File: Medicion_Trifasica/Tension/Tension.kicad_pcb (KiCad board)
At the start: 4 copper layers, 60.5 x 22.5 mm, 14 parts, among them IC1 ADR130BUJZ-REEL7, J1 Screw_Terminal_01x02, J2 Conn_01x02_Pin, J3 Conn_01x02_Pin, T1 Transformer_220/9, U1 LM358

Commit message: Mejoras PCB medicion tension
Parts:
- moved C1 92.1 mm to (168.5, 100.3)
- moved C2 92.1 mm to (156.2, 99.2)
- moved C3 92.1 mm to (162.2, 99.2)
- moved IC1 92.1 mm to (159.2, 98.7)
- moved J1 92.1 mm to (126.3, 107.8)
- moved J3 92.1 mm to (169.3, 113.6)
- moved R1 92.1 mm to (155.0, 103.6)
- moved R2 92.1 mm to (155.0, 108.1)
- moved R3 92.1 mm to (159.0, 104.6)
- moved R4 92.1 mm to (163.0, 103.6)
- moved R5 92.1 mm to (168.5, 98.1)
- moved T1 92.1 mm to (146.8, 101.8)
- moved U1 92.1 mm to (168.6, 105.1)
- moved J2 88.3 mm to (175.1, 104.6)
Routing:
- net Net-(J2-Pin_1): track 21.1 -> 16.4 mm
- net GND: track 50.1 -> 45.4 mm
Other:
- board size 60.5 x 22.5 mm -> 55.8 x 22.5 mm

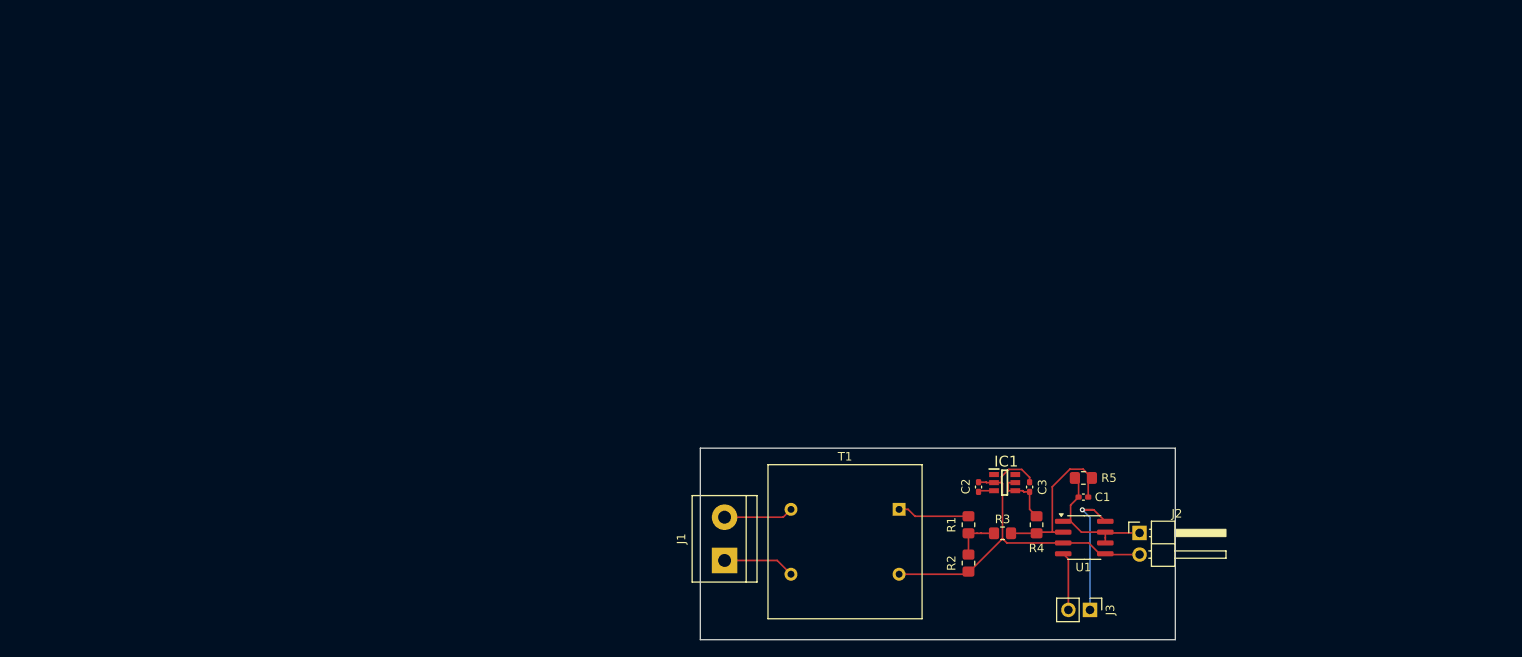
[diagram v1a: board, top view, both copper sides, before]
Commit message: Correciones PCBs
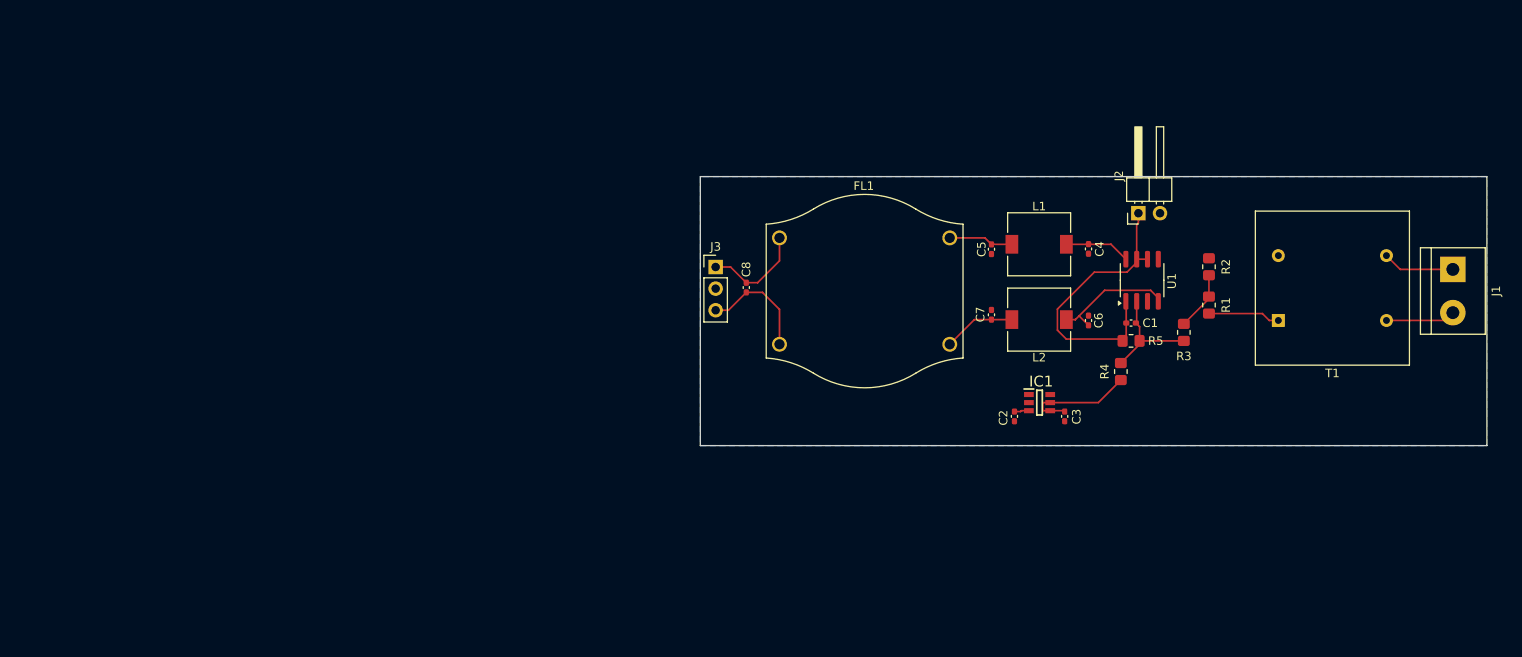
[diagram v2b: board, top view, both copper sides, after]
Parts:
- added C4: 100 nF, Capacitor_SMD:C_0402_1005Metric_Pad0.74x0.62mm_HandSolder, F.Cu at (169.1, 71.2)
- added C5: 100 nF, Capacitor_SMD:C_0402_1005Metric_Pad0.74x0.62mm_HandSolder, F.Cu at (157.7, 71.2)
- added C6: 100 nF, Capacitor_SMD:C_0402_1005Metric_Pad0.74x0.62mm_HandSolder, F.Cu at (169.1, 79.6)
- added C7: 100 nF, Capacitor_SMD:C_0402_1005Metric_Pad0.74x0.62mm_HandSolder, F.Cu at (157.7, 78.9)
- added C8: 470 uF, Capacitor_SMD:C_0402_1005Metric_Pad0.74x0.62mm_HandSolder, F.Cu at (128.9, 75.7)
- added FL1: Choke_CommonMode_FerriteCore_1234, Inductor_THT:Choke_EPCOS_B82722A, F.Cu at (132.8, 69.9)
- added L1: 30 uH, Inductor_SMD:L_7.3x7.3_H3.5, F.Cu at (163.3, 70.7)
- added L2: 30 uH, Inductor_SMD:L_7.3x7.3_H3.5, F.Cu at (163.3, 79.5)
- J3: value Conn_01x02_Pin -> Conn_01x03_Pin; footprint Connector_PinHeader_2.54mm:PinHeader_1x02_P2.54mm_Vertical -> Connector_PinHeader_2.54mm:PinHeader_1x03_P2.54mm_Vertical
- moved J1 92.1 mm to (211.9, 73.6), turned to -90 degrees
- moved J3 59.6 mm to (125.3, 73.3), turned to 0 degrees
- moved T1 49.8 mm to (191.4, 79.6), turned to 180 degrees
- moved R2 44.8 mm to (183.2, 73.3), turned to 90 degrees
- moved R1 38.3 mm to (183.2, 77.8), turned to 90 degrees
- moved J2 37.6 mm to (175.0, 67.0), turned to 90 degrees
- moved R3 31.8 mm to (180.3, 81.0), turned to -90 degrees
- moved U1 31.0 mm to (175.4, 74.9), turned to 90 degrees
- moved C1 21.2 mm to (174.1, 79.9)
- moved R4 20.5 mm to (172.9, 85.6), turned to 90 degrees
- moved R5 17.0 mm to (174.1, 82.0)
- moved IC1 10.3 mm to (163.3, 89.2)
- moved C2 9.31 mm to (160.4, 90.9), turned to -90 degrees
- moved C3 9.27 mm to (166.3, 90.9), turned to -90 degrees
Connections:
- J3 pad 2: Net-(J3-Pin_2) -> GND
- U1 pad 4: Net-(J3-Pin_2) -> Net-(U1C-V-)
- U1 pad 8: Net-(J3-Pin_1) -> +9V
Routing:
- net GND: track 45.4 -> 0.44 mm
- net Net-(J2-Pin_1): track 16.4 -> 34.1 mm
- net Net-(U1C-V-): track 0.00 -> 14.6 mm
- net Net-(J3-Pin_3): track 0.00 -> 13.3 mm
- net Net-(C7-Pad2): track 0.00 -> 8.50 mm
- net +9V: track 1.87 -> 9.67 mm
- net Net-(J3-Pin_1): track 20.5 -> 12.8 mm, vias 1 -> 0
- net Net-(C5-Pad2): track 0.00 -> 7.62 mm
- net Net-(J3-Pin_2): track 6.85 -> 0.00 mm
- net Net-(U1A--): track 19.9 -> 13.6 mm
- net VDC_0.5: track 7.65 -> 13.8 mm
- net Net-(R1-Pad2): track 5.50 -> 6.93 mm
- added copper zone on B.Cu, net GND
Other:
- board size 55.8 x 22.5 mm -> 92.4 x 31.6 mm
- copper layers 4 -> 2

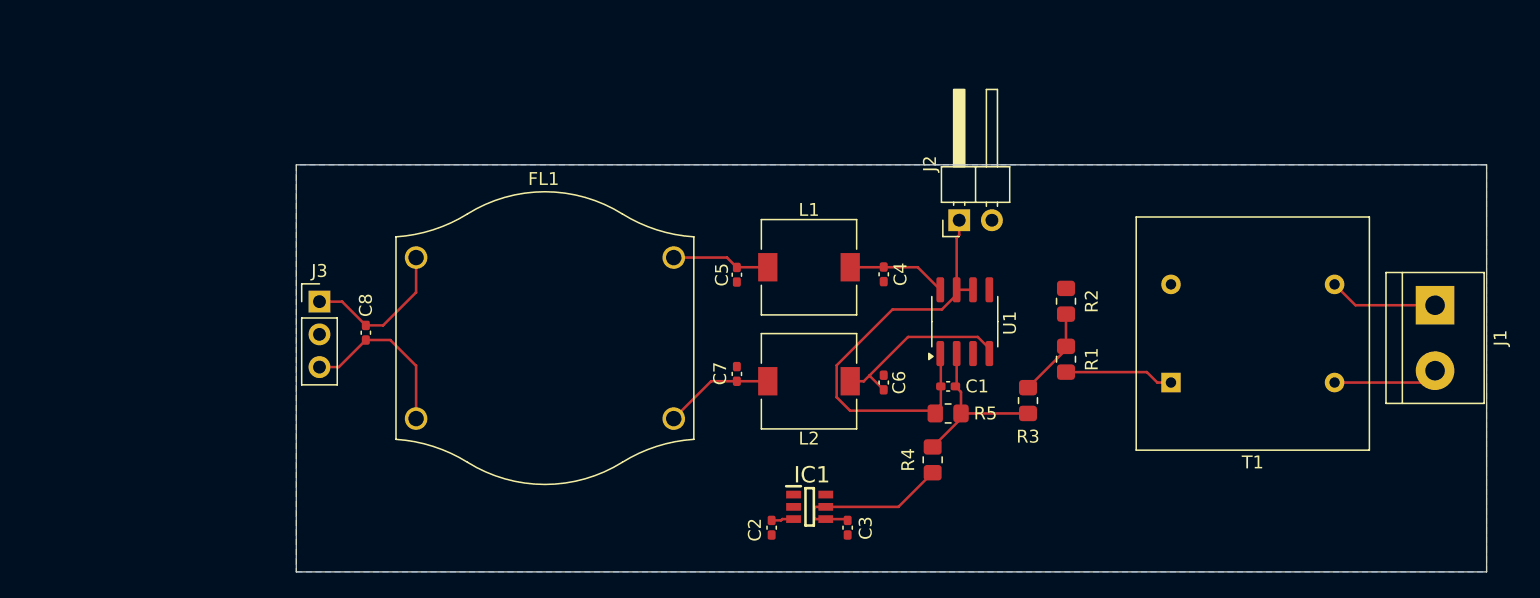
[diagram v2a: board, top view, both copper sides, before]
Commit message: Mejora en la organizacion de los circuitos con netclases y colores
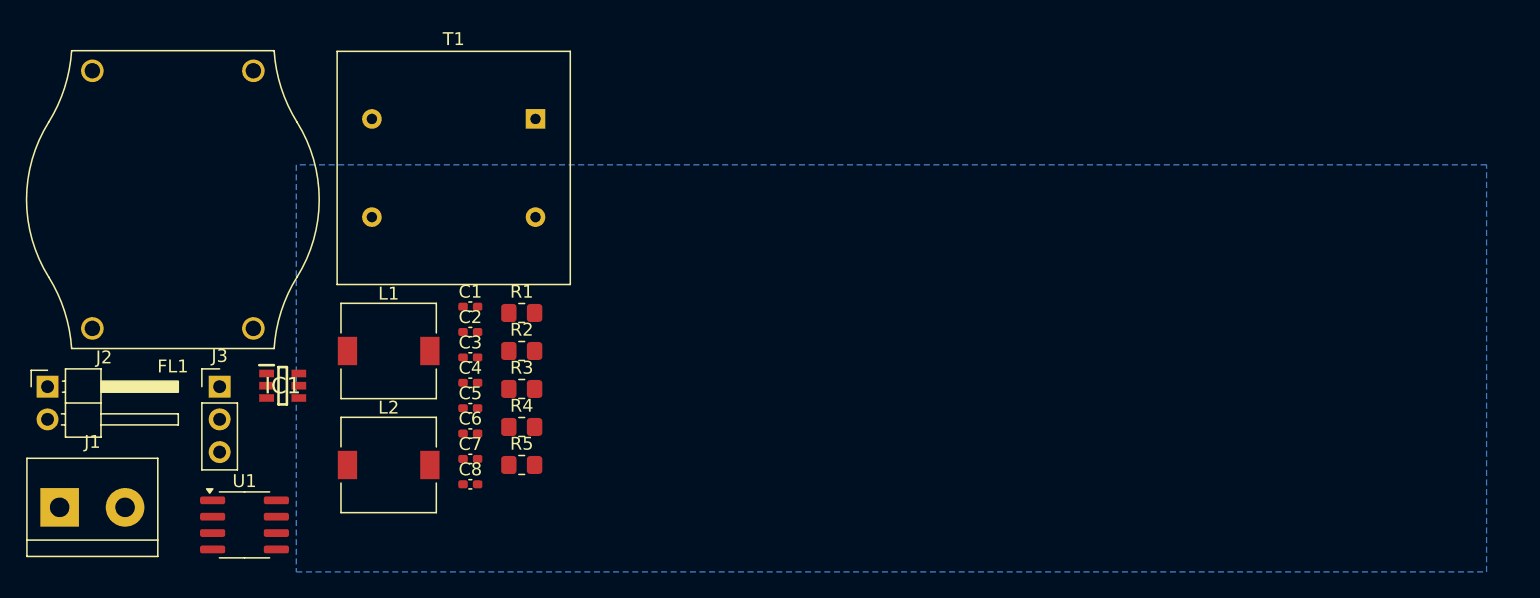
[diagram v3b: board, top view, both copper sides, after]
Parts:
- moved J1 107.9 mm to (105.1, 89.3), turned to 0 degrees
- moved J2 71.9 mm to (104.2, 79.9), turned to 0 degrees
- moved U1 58.1 mm to (119.5, 90.7), turned to 0 degrees
- moved T1 53.4 mm to (142.1, 59.1), turned to 0 degrees
- moved R2 42.4 mm to (141.0, 77.2), turned to 0 degrees
- moved R1 42.4 mm to (141.0, 74.2), turned to 0 degrees
- moved IC1 42.0 mm to (122.4, 79.8)
- moved R3 39.3 mm to (141.0, 80.1), turned to 0 degrees
- moved C1 37.6 mm to (137.0, 73.7), turned to 0 degrees
- moved R5 33.3 mm to (141.0, 86.0), turned to 0 degrees
- moved L1 33.3 mm to (130.7, 77.2)
- moved L2 33.3 mm to (130.7, 86.0), turned to 0 degrees
- moved C4 33.2 mm to (137.0, 79.6), turned to 0 degrees
- moved C6 32.3 mm to (137.0, 83.6), turned to 0 degrees
- moved C3 32.1 mm to (137.0, 77.7), turned to 0 degrees
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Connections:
- net Net-(J1-Pin_1) renamed /AC-
- net Net-(J1-Pin_2) renamed /AC+
- net Net-(J2-Pin_1) renamed /Voltage_O_Buffer
- net Net-(J3-Pin_1) renamed /Input_+9V
- net Net-(J3-Pin_3) renamed /Input_-9V
- net Net-(R1-Pad2) renamed /Voltage_Div
- net Net-(U1A--) renamed /AO_SUM_e+
- net Net-(U1C-V-) renamed /-9V
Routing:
- net /Voltage_O_Buffer: track 34.1 -> 0.00 mm
- net /-9V: track 14.6 -> 0.00 mm
- net VDC_0.5: track 13.8 -> 0.00 mm
- net /AO_SUM_e+: track 13.6 -> 0.00 mm
- net /Input_-9V: track 13.3 -> 0.00 mm
- net /Input_+9V: track 12.8 -> 0.00 mm
- net +9V: track 9.67 -> 0.00 mm
- net Net-(C7-Pad2): track 8.50 -> 0.00 mm
- net Net-(T1-SB): track 8.49 -> 0.00 mm
- net /AC-: track 8.47 -> 0.00 mm
- net /AC+: track 8.18 -> 0.00 mm
- net Net-(C5-Pad2): track 7.62 -> 0.00 mm
- net /Voltage_Div: track 6.93 -> 0.00 mm
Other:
- board outline removed

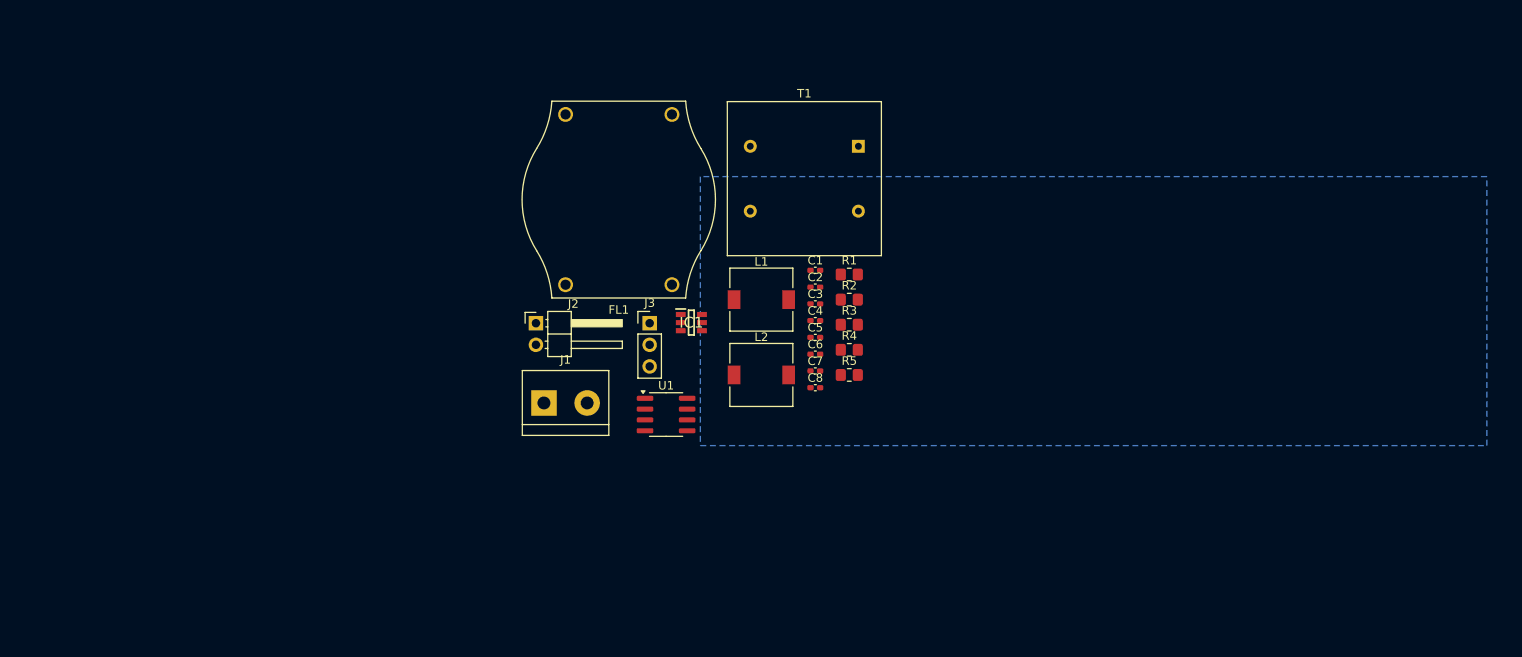
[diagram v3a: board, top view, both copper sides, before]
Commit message: Reconexión de la PCB, y terminación de conexiones
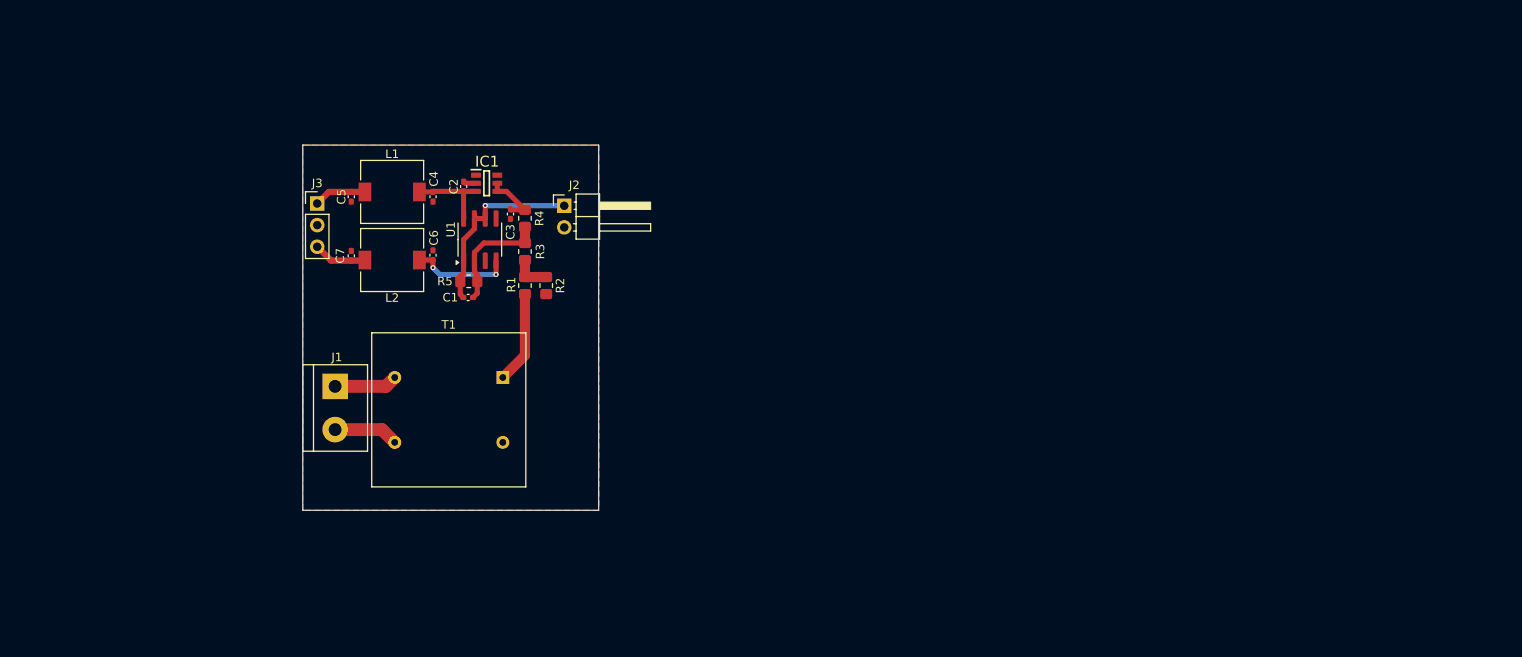
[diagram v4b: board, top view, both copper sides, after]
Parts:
- removed C8: 470 uF, Capacitor_SMD:C_0402_1005Metric_Pad0.74x0.62mm_HandSolder
- removed FL1: Choke_CommonMode_FerriteCore_1234, Inductor_THT:Choke_EPCOS_B82722A
- moved C5 57.0 mm to (82.5, 65.1), turned to 90 degrees
- moved C7 56.2 mm to (82.5, 72.0), turned to -90 degrees
- moved T1 49.8 mm to (100.3, 86.3)
- moved C4 47.2 mm to (92.1, 65.1), turned to 90 degrees
- moved C6 46.4 mm to (92.1, 71.9), turned to -90 degrees
- moved R5 46.0 mm to (96.3, 75.0), turned to 180 degrees
- moved L2 45.4 mm to (87.3, 72.5), turned to 180 degrees
- moved L1 45.2 mm to (87.3, 64.5)
- moved C2 43.0 mm to (95.7, 63.9), turned to 90 degrees
- moved J3 41.5 mm to (78.5, 65.9)
- moved R4 41.1 mm to (102.9, 67.6), turned to -90 degrees
- moved C1 40.9 mm to (96.2, 76.9), turned to 180 degrees
- moved R3 39.1 mm to (102.9, 71.5), turned to 90 degrees
- moved R1 38.1 mm to (102.9, 75.5), turned to 90 degrees
- moved C3 37.3 mm to (101.2, 67.1), turned to -90 degrees
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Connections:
- C5 pad 2: Net-(C5-Pad2) -> /Input_+9V
- C7 pad 2: Net-(C7-Pad2) -> /Input_-9V
- J1 pad 1: /AC- -> /AC+
- J1 pad 2: /AC+ -> /AC-
- L1 pad 1: Net-(C5-Pad2) -> /Input_+9V
- L2 pad 2: Net-(C7-Pad2) -> /Input_-9V
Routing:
- net /Voltage_O_Buffer: track 0.00 -> 22.3 mm, vias 0 -> 1
- net /AO_SUM_e+: track 0.00 -> 13.9 mm
- net /-9V: track 0.00 -> 11.9 mm, vias 0 -> 2
- net Net-(T1-SB): track 0.00 -> 10.9 mm
- net +9V: track 0.00 -> 10.1 mm
- net /AC-: track 0.00 -> 7.62 mm
- net /AC+: track 0.00 -> 7.43 mm
- net VDC_0.5: track 0.00 -> 6.82 mm
- net /Input_-9V: track 0.00 -> 6.30 mm
- net /Input_+9V: track 0.00 -> 6.16 mm
- net /Voltage_Div: track 0.00 -> 4.50 mm
- net GND: track 0.00 -> 1.53 mm
- added copper zone on F.Cu, net GND
- removed copper zone on B.Cu, net GND
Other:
- board outline added: 34.8 x 42.9 mm
